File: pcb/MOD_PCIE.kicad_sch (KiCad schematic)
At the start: 18 parts, among them J7 2041262-1, SW2 SW_DIP_x02

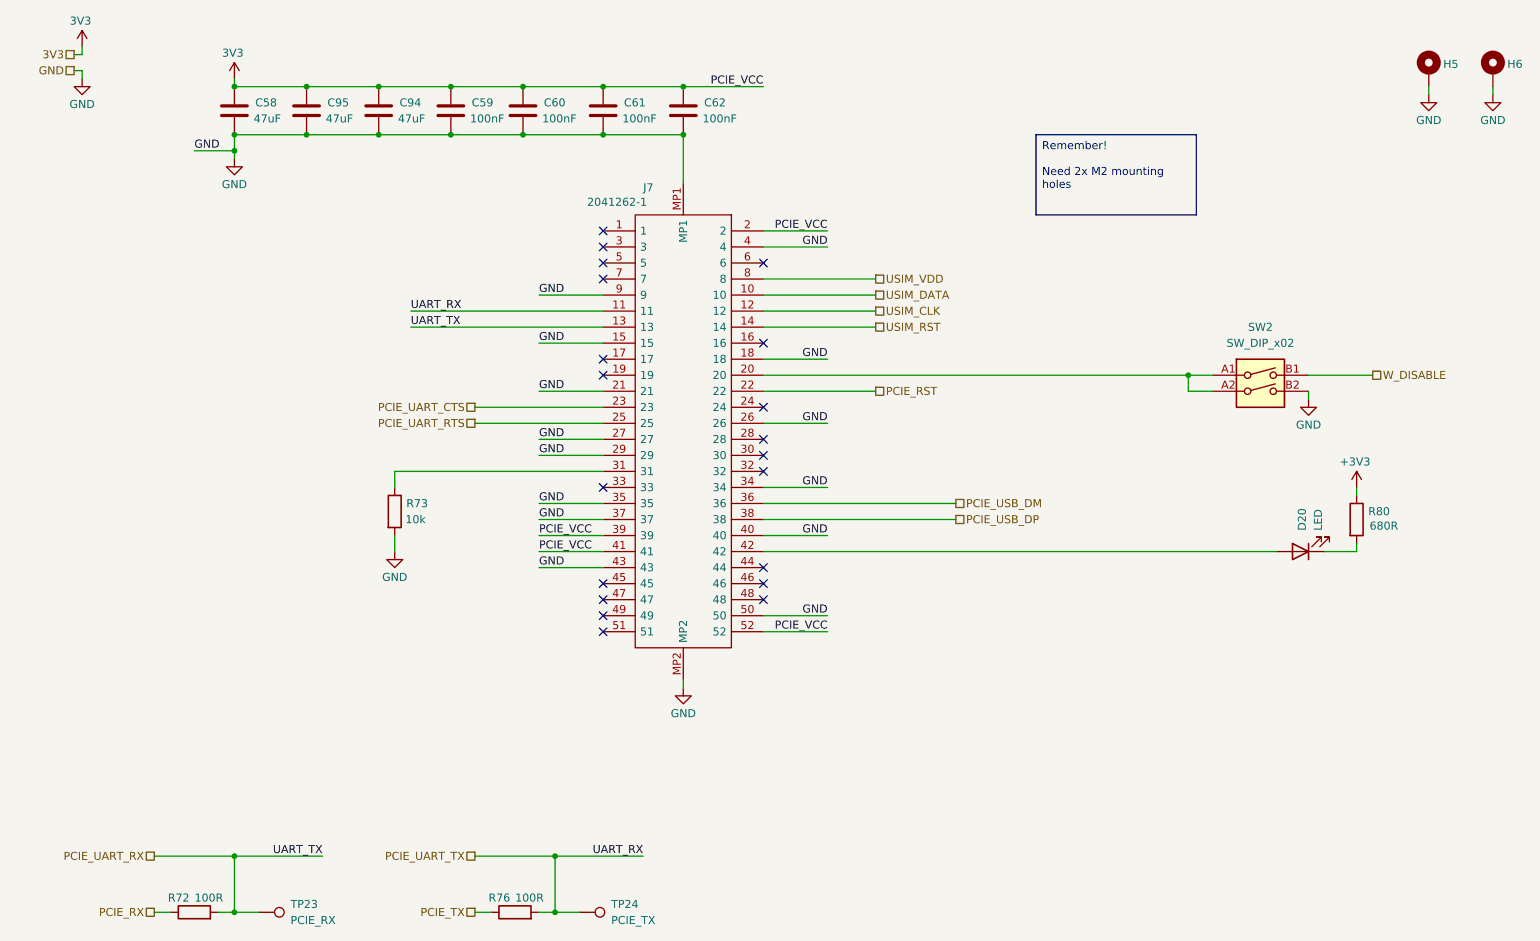
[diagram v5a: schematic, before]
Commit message: initial routing of power for pcie, swapped switches for jumpers
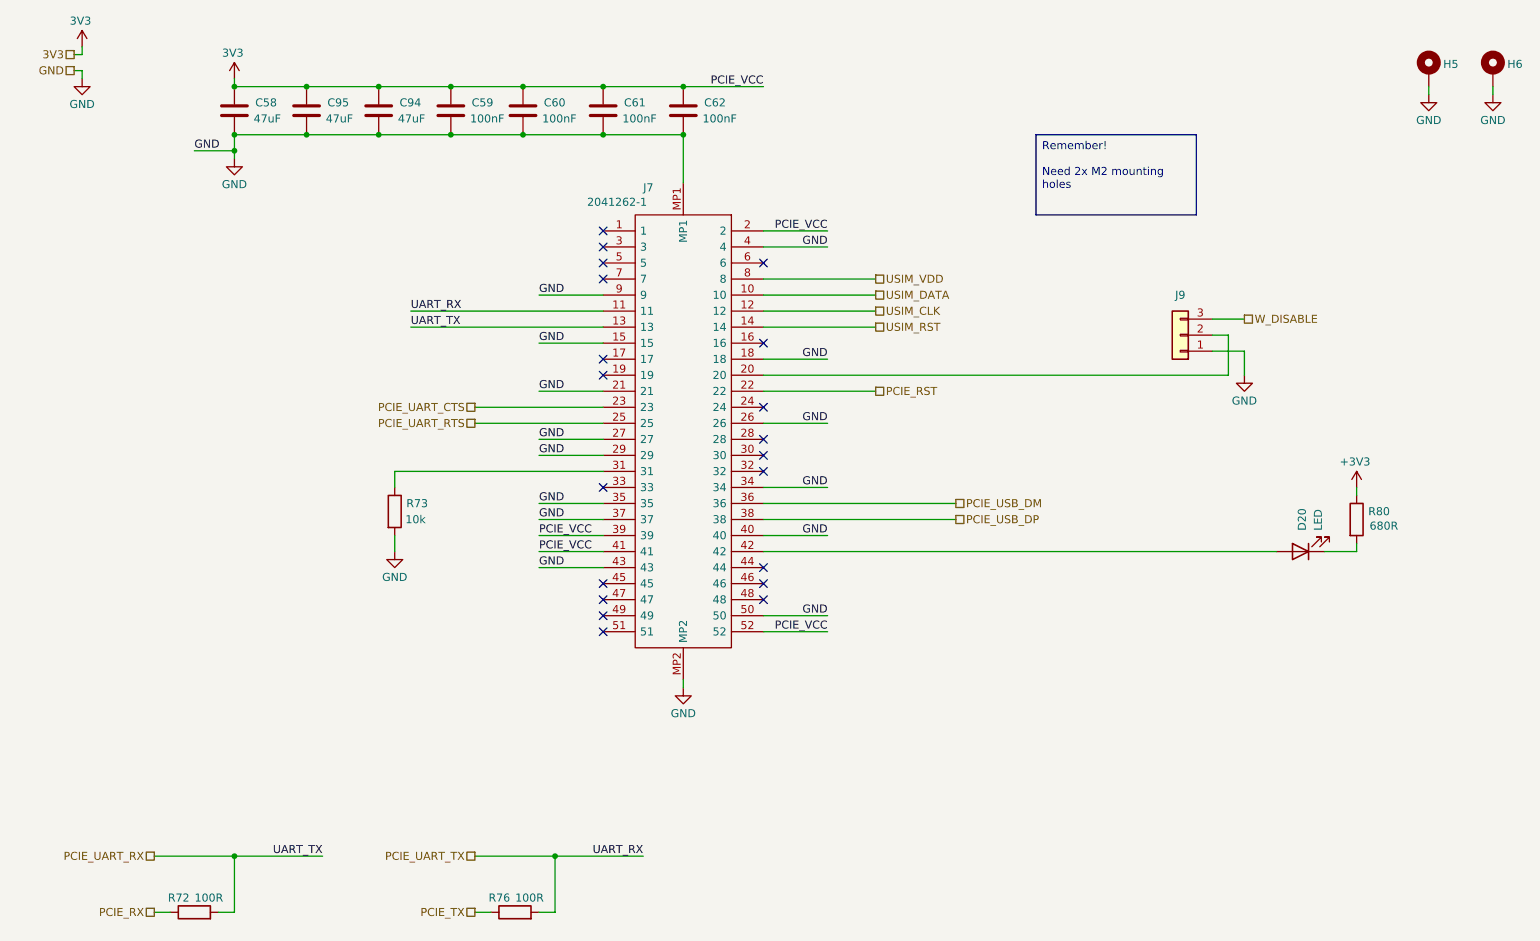
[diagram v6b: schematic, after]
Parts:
- removed SW2: SW_DIP_x02, SamacSys_Parts:EDS02SNRNTR04Q, symbol Switch:SW_DIP_x02
- removed TP23: PCIE_RX, TestPoint:TestPoint_THTPad_D2.0mm_Drill1.0mm, symbol Connector:TestPoint
- removed TP24: PCIE_TX, TestPoint:TestPoint_THTPad_D2.0mm_Drill1.0mm, symbol Connector:TestPoint
- added J9: Conn_01x03, Connector_PinHeader_2.54mm:PinHeader_1x03_P2.54mm_Vertical, symbol Connector_Generic:Conn_01x03
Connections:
- net GND: now also J9.1 (Pin_1)
- net W_DISABLE: now also J9.3 (Pin_3)
- net at J7.20: now also J9.2 (Pin_2)
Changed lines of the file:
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@@
 	)
 	(junction
-		(at 201.93 76.2)
-		(diameter 0)
-		(color 0 0 0 0)
-	)
-	(junction
 		(at 109.22 38.1)
 		(diameter 0)
@@
 	)
 	(junction
-		(at 50.8 161.29)
-		(diameter 0)
-		(color 0 0 0 0)
-	)
-	(junction
 		(at 62.23 30.48)
 		(diameter 0)
@@
 	)
 	(junction
-		(at 101.6 161.29)
-		(diameter 0)
-		(color 0 0 0 0)
-	)
-	(junction
 		(at 62.23 38.1)
 		(diameter 0)
@@
 	(wire
 		(pts
-			(xy 50.8 161.29) (xy 54.61 161.29)
+			(xy 208.28 76.2) (xy 208.28 69.85)
 		)
 		(stroke
@@
 	(wire
 		(pts
+			(xy 208.28 69.85) (xy 205.74 69.85)
+		)
+		(stroke
+			(width 0)
+			(type default)
+		)
+	)
+	(wire
+		(pts
 			(xy 76.2 91.44) (xy 76.2 93.98)
 		)
@@
 	(wire
 		(pts
-			(xy 201.93 78.74) (xy 201.93 76.2)
+			(xy 205.74 67.31) (xy 210.82 67.31)
 		)
 		(stroke
@@
 	(wire
 		(pts
-			(xy 220.98 76.2) (xy 231.14 76.2)
+			(xy 73.66 38.1) (xy 85.09 38.1)
 		)
 		(stroke
@@
 	(wire
 		(pts
-			(xy 73.66 38.1) (xy 85.09 38.1)
+			(xy 134.62 101.6) (xy 144.78 101.6)
 		)
 		(stroke
@@
 	(wire
 		(pts
-			(xy 134.62 101.6) (xy 144.78 101.6)
+			(xy 210.82 72.39) (xy 205.74 72.39)
 		)
 		(stroke
@@
 	(wire
 		(pts
-			(xy 101.6 161.29) (xy 105.41 161.29)
-		)
-		(stroke
-			(width 0)
-			(type default)
-		)
-	)
-	(wire
-		(pts
 			(xy 109.22 91.44) (xy 76.2 91.44)
 		)
@@
 	(wire
 		(pts
-			(xy 134.62 76.2) (xy 201.93 76.2)
+			(xy 134.62 76.2) (xy 208.28 76.2)
 		)
 		(stroke
@@
 	(wire
 		(pts
-			(xy 201.93 76.2) (xy 205.74 76.2)
-		)
-		(stroke
-			(width 0)
-			(type default)
-		)
-	)
-	(wire
-		(pts
 			(xy 50.8 38.1) (xy 62.23 38.1)
 		)
@@
 	(wire
 		(pts
-			(xy 205.74 78.74) (xy 201.93 78.74)
-		)
-		(stroke
-			(width 0)
-			(type default)
-		)
-	)
-	(wire
-		(pts
 			(xy 228.6 93.98) (xy 228.6 95.25)
 		)
@@
 	(wire
 		(pts
-			(xy 220.98 78.74) (xy 220.98 80.01)
+			(xy 210.82 72.39) (xy 210.82 76.2)
 		)
 		(stroke
@@
 	(hierarchical_label "W_DISABLE"
 		(shape passive)
-		(at 231.14 76.2 0)
+		(at 210.82 67.31 0)
 		(effects
 			(font
@@
 	)
 	(symbol
-		(lib_id "Connector:TestPoint")
-		(at 105.41 161.29 270)
-		(unit 1)
-		(exclude_from_sim no)
-		(in_bom yes)
-		(on_board yes)
-		(dnp no)
-		(fields_autoplaced yes)
-		(property "Reference" "TP24"
-			(at 110.49 160.0199 90)
-			(effects
-				(font
-					(size 1.27 1.27)
-				)
-				(justify left)
-			)
-		)
-		(property "Value" "PCIE_TX"
-			(at 110.49 162.5599 90)
-			(effects
-				(font
-					(size 1.27 1.27)
-				)
-				(justify left)
-			)
-		)
-		(property "Footprint" "TestPoint:TestPoint_THTPad_D2.0mm_Drill1.0mm"
-			(at 105.41 166.37 0)
-			(effects
-				(font
-					(size 1.27 1.27)
-				)
-				(hide yes)
-			)
-		)
-		(property "Datasheet" "~"
-			(at 105.41 166.37 0)
-			(effects
-				(font
-					(size 1.27 1.27)
-				)
-				(hide yes)
-			)
-		)
-		(property "Description" "test point"
-			(at 105.41 161.29 0)
-			(effects
-				(font
-					(size 1.27 1.27)
-				)
-				(hide yes)
-			)
-		)
-		(pin "1"
-		)
-		(instances
-			(project "NCU"
-				(path "/3aee14c3-5480-4f7c-989e-3fef81779034/77f505d1-5a70-4b67-92f2-4570e0aae5e4"
-					(reference "TP24")
-					(unit 1)
-				)
-			)
-		)
-	)
-	(symbol
 		(lib_id "power:+5V")
 		(at 50.8 29.21 0)
@@
 	)
 	(symbol
+		(lib_id "Connector_Generic:Conn_01x03")
+		(at 200.66 69.85 180)
+		(unit 1)
+		(exclude_from_sim no)
+		(in_bom yes)
+		(on_board yes)
+		(dnp no)
+		(fields_autoplaced yes)
+		(property "Reference" "J9"
+			(at 200.66 63.5 0)
+			(effects
+				(font
+					(size 1.27 1.27)
+				)
+			)
+		)
+		(property "Value" "Conn_01x03"
+			(at 199.3901 74.93 90)
+			(effects
+				(font
+					(size 1.27 1.27)
+				)
+				(justify left)
+				(hide yes)
+			)
+		)
+		(property "Footprint" "Connector_PinHeader_2.54mm:PinHeader_1x03_P2.54mm_Vertical"
+			(at 200.66 69.85 0)
+			(effects
+				(font
+					(size 1.27 1.27)
+				)
+				(hide yes)
+			)
+		)
+		(property "Datasheet" "~"
+			(at 200.66 69.85 0)
+			(effects
+				(font
+					(size 1.27 1.27)
+				)
+				(hide yes)
+			)
+		)
+		(property "Description" "Generic connector, single row, 01x03, script generated (kicad-library-utils/schlib/autogen/connector/)"
+			(at 200.66 69.85 0)
+			(effects
+				(font
+					(size 1.27 1.27)
+				)
+				(hide yes)
+			)
+		)
+		(pin "1"
+		)
+		(pin "3"
+		)
+		(pin "2"
+		)
+		(instances
+			(project ""
+				(path "/3aee14c3-5480-4f7c-989e-3fef81779034/77f505d1-5a70-4b67-92f2-4570e0aae5e4"
+					(reference "J9")
+					(unit 1)
+				)
+			)
+		)
+	)
+	(symbol
 		(lib_id "power:GND")
 		(at 240.03 31.75 0)
@@
 	(symbol
 		(lib_id "power:GND")
-		(at 220.98 80.01 0)
+		(at 210.82 76.2 0)
 		(mirror y)
 		(unit 1)
@@
 		(dnp no)
 		(property "Reference" "#PWR0304"
-			(at 220.98 86.36 0)
+			(at 210.82 82.55 0)
 			(effects
 				(font
@@
 		)
 		(property "Value" "GND"
-			(at 220.98 84.074 0)
+			(at 210.82 80.264 0)
 			(effects
 				(font
@@
 		)
 		(property "Footprint" ""
-			(at 220.98 80.01 0)
+			(at 210.82 76.2 0)
 			(effects
 				(font
@@
 		)
 		(property "Datasheet" ""
-			(at 220.98 80.01 0)
+			(at 210.82 76.2 0)
 			(effects
 				(font
@@
 		)
 		(property "Description" "Power symbol creates a global label with name \"GND\" , ground"
-			(at 220.98 80.01 0)
+			(at 210.82 76.2 0)
 			(effects
 				(font
@@
 	)
 	(symbol
-		(lib_id "Switch:SW_DIP_x02")
-		(at 213.36 78.74 0)
-		(unit 1)
-		(exclude_from_sim no)
-		(in_bom yes)
-		(on_board yes)
-		(dnp no)
-		(fields_autoplaced yes)
-		(property "Reference" "SW2"
-			(at 213.36 68.58 0)
-			(effects
-				(font
-					(size 1.27 1.27)
-				)
-			)
-		)
-		(property "Value" "SW_DIP_x02"
-			(at 213.36 71.12 0)
-			(effects
-				(font
-					(size 1.27 1.27)
-				)
-			)
-		)
-		(property "Footprint" "SamacSys_Parts:EDS02SNRNTR04Q"
-			(at 213.36 78.74 0)
-			(effects
-				(font
-					(size 1.27 1.27)
-				)
-				(hide yes)
-			)
-		)
-		(property "Datasheet" "~"
-			(at 213.36 78.74 0)
-			(effects
-				(font
-					(size 1.27 1.27)
-				)
-				(hide yes)
-			)
-		)
-		(property "Description" "2x DIP Switch, Single Pole Single Throw (SPST) switch, small symbol"
-			(at 213.36 78.74 0)
-			(effects
-				(font
-					(size 1.27 1.27)
-				)
-				(hide yes)
-			)
-		)
-		(pin "A1"
-		)
-		(pin "B2"
-		)
-		(pin "A2"
-		)
-		(pin "B1"
-		)
-		(instances
-			(project ""
-				(path "/3aee14c3-5480-4f7c-989e-3fef81779034/77f505d1-5a70-4b67-92f2-4570e0aae5e4"
-					(reference "SW2")
-					(unit 1)
-				)
-			)
-		)
-	)
-	(symbol
 		(lib_id "power:GND")
 		(at 50.8 41.91 0)
@@
 					(unit 1)
 				)
-			)
-		)
-	)
-	(symbol
-		(lib_id "Connector:TestPoint")
-		(at 54.61 161.29 270)
-		(unit 1)
-		(exclude_from_sim no)
-		(in_bom yes)
-		(on_board yes)
-		(dnp no)
-		(fields_autoplaced yes)
-		(property "Reference" "TP23"
-			(at 59.69 160.0199 90)
-			(effects
-				(font
-					(size 1.27 1.27)
-				)
-				(justify left)
-			)
-		)
-		(property "Value" "PCIE_RX"
-			(at 59.69 162.5599 90)
-			(effects
-				(font
-					(size 1.27 1.27)
-				)
-				(justify left)
-			)
-		)
-		(property "Footprint" "TestPoint:TestPoint_THTPad_D2.0mm_Drill1.0mm"
-			(at 54.61 166.37 0)
-			(effects
-				(font
-					(size 1.27 1.27)
-				)
-				(hide yes)
-			)
-		)
-		(property "Datasheet" "~"
-			(at 54.61 166.37 0)
-			(effects
-				(font
-					(size 1.27 1.27)
-				)
-				(hide yes)
-			)
-		)
-		(property "Description" "test point"
-			(at 54.61 161.29 0)
-			(effects
-				(font
-					(size 1.27 1.27)
-				)
-				(hide yes)
-			)
-		)
-		(pin "1"
-		)
-		(instances
-			(project "NCU"
-				(path "/3aee14c3-5480-4f7c-989e-3fef81779034/77f505d1-5a70-4b67-92f2-4570e0aae5e4"
-					(reference "TP23")
-					(unit 1)
-				)

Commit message: initial drc warnings complete
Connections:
- net +3V3 is gone; now on net 3V3: R80.1
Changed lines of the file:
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@@
 			)
 		)
-		(property "Value" "+3V3"
+		(property "Value" "3V3"
 			(at 228.346 89.916 0)
 			(effects

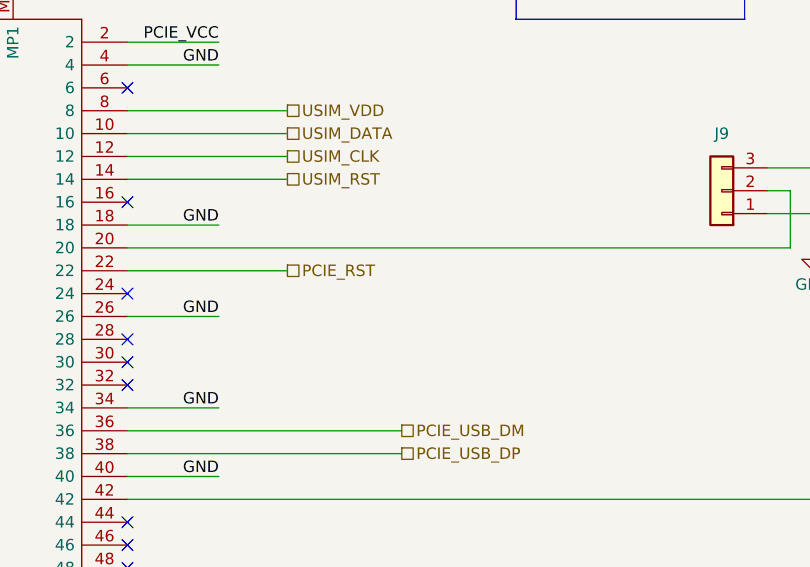
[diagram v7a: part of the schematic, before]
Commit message: added jumper to external PCIE reset line. removed arrayed component ids and replaced with instance labels
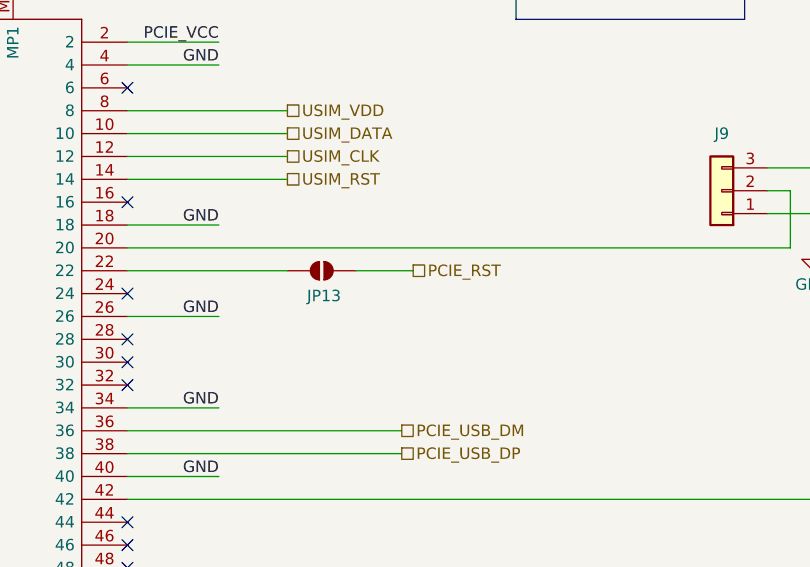
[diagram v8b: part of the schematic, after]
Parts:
- added JP13: SolderJumper_2_Open, Jumper:SolderJumper-2_P1.3mm_Open_RoundedPad1.0x1.5mm, symbol Jumper:SolderJumper_2_Open
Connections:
- net PCIE_RST: now also JP13.2 (B); no longer J7.22
- new net: J7.22, JP13.1 (A)
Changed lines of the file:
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@@
+	(wire
+		(pts
+			(xy 160.02 78.74) (xy 166.37 78.74)
+		)
+		(stroke
+			(width 0)
+			(type default)
+		)
+	)
 	(wire
 		(pts
@@
 	(hierarchical_label "PCIE_RST"
 		(shape passive)
-		(at 152.4 78.74 0)
+		(at 166.37 78.74 0)
 		(effects
 			(font
@@
 					(unit 1)
 				)
+			)
+		)
+	)
+	(symbol
+		(lib_id "Jumper:SolderJumper_2_Open")
+		(at 156.21 78.74 0)
+		(mirror x)
+		(unit 1)
+		(exclude_from_sim no)
+		(in_bom no)
+		(on_board yes)
+		(dnp no)
+		(property "Reference" "JP13"
+			(at 156.464 81.534 0)
+			(effects
+				(font
+					(size 1.27 1.27)
+				)
+			)
+		)
+		(property "Value" "SolderJumper_2_Open"
+			(at 156.21 82.55 0)
+			(effects
+				(font
+					(size 1.27 1.27)
+				)
+				(hide yes)
+			)
+		)
+		(property "Footprint" "Jumper:SolderJumper-2_P1.3mm_Open_RoundedPad1.0x1.5mm"
+			(at 156.21 78.74 0)
+			(effects
+				(font
+					(size 1.27 1.27)
+				)
+				(hide yes)
+			)
+		)
+		(property "Datasheet" "~"
+			(at 156.21 78.74 0)
+			(effects
+				(font
+					(size 1.27 1.27)
+				)
+				(hide yes)
+			)
+		)
+		(property "Description" "Solder Jumper, 2-pole, open"
+			(at 156.21 78.74 0)
+			(effects
+				(font
+					(size 1.27 1.27)
+				)
+				(hide yes)
+			)
+		)
+		(pin "2"
+		)
+		(pin "1"
+		)
+		(instances
+			(project "NCU"
+				(path "/3aee14c3-5480-4f7c-989e-3fef81779034/77f505d1-5a70-4b67-92f2-4570e0aae5e4"
+					(reference "JP13")
+					(unit 1)
+				)
